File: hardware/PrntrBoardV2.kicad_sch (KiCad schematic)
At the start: 13 parts

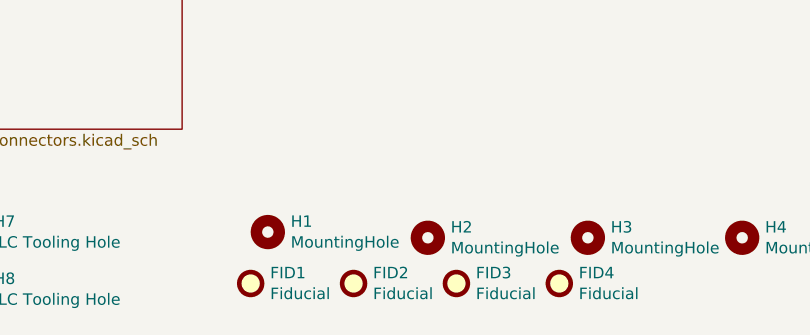
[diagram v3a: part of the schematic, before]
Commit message: Added separate power supply for motor drivers, to accomodate high voltage driver versions.
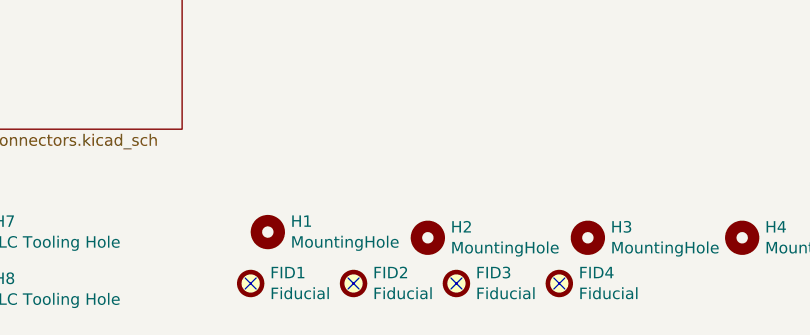
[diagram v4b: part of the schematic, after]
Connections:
- no-connect marks 0 -> 4
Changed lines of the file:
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@@
 (kicad_sch (version 20210621) (generator eeschema)
   (paper "A4")
+  (no_connect (at 196.215 157.48))
+  (no_connect (at 207.645 157.48))
+  (no_connect (at 219.075 157.48))
+  (no_connect (at 230.505 157.48))
   (symbol (lib_id "Mechanical:Fiducial") (at 196.215 157.48 0) (unit 1)
     (in_bom no) (on_board yes)
@@
       (reference "#PWR077") (unit 1) (value "GND") (footprint "")
     )
+    (path "/00000000-0000-0000-0000-00005db03b7d/9aa42597-a571-49ba-a769-f65a412defcf"
+      (reference "#PWR078") (unit 1) (value "GND") (footprint "")
+    )
+    (path "/00000000-0000-0000-0000-00005db03b7d/f7e58a64-e7a2-485d-858e-ff6a326b8d61"
+      (reference "#PWR079") (unit 1) (value "GND") (footprint "")
+    )
     (path "/00000000-0000-0000-0000-00005dabbbab/00000000-0000-0000-0000-00005daf7240"
       (reference "#PWR0101") (unit 1) (value "GND") (footprint "")
@@
       (reference "#PWR0104") (unit 1) (value "GND") (footprint "")
     )
+    (path "/00000000-0000-0000-0000-00005dabbbab/8844a2b1-600f-4d16-a024-4570839840b9"
+      (reference "#PWR0105") (unit 1) (value "GNDA") (footprint "")
+    )
     (path "/00000000-0000-0000-0000-00005dabbbab/00000000-0000-0000-0000-00005dabc8ef"
       (reference "C1") (unit 1) (value "0.1uF") (footprint "PrntrBoardV2:C_0603_1608Metric")
@@
       (reference "C46") (unit 1) (value "0.1uF") (footprint "PrntrBoardV2:C_0603_1608Metric")
     )
-    (path "/00000000-0000-0000-0000-00005dace5fc/00000000-0000-0000-0000-00005db2f31b"
-      (reference "C47") (unit 1) (value "100uF 35V") (footprint "Capacitor_SMD:CP_Elec_6.3x7.7")
-    )
-    (path "/00000000-0000-0000-0000-00005dace5fc/00000000-0000-0000-0000-00005db33ffa"
-      (reference "C48") (unit 1) (value "100uF 35V") (footprint "Capacitor_SMD:CP_Elec_6.3x7.7")
-    )
-    (path "/00000000-0000-0000-0000-00005dace5fc/00000000-0000-0000-0000-00005db326a1"
-      (reference "C49") (unit 1) (value "100uF 35V") (footprint "Capacitor_SMD:CP_Elec_6.3x7.7")
-    )
-    (path "/00000000-0000-0000-0000-00005dace5fc/00000000-0000-0000-0000-00005db3478c"
-      (reference "C50") (unit 1) (value "100uF 35V") (footprint "Capacitor_SMD:CP_Elec_6.3x7.7")
-    )
-    (path "/00000000-0000-0000-0000-00005dace5fc/00000000-0000-0000-0000-00005db32f14"
-      (reference "C51") (unit 1) (value "100uF 35V") (footprint "Capacitor_SMD:CP_Elec_6.3x7.7")
-    )
-    (path "/00000000-0000-0000-0000-00005dace5fc/00000000-0000-0000-0000-00005db339e2"
-      (reference "C52") (unit 1) (value "100uF 35V") (footprint "Capacitor_SMD:CP_Elec_6.3x7.7")
+    (path "/00000000-0000-0000-0000-00005dace5fc/f1cb98d4-956f-4cdb-a90e-6df52427c521"
+      (reference "C47") (unit 1) (value "4.7uF 100V") (footprint "Capacitor_SMD:C_1210_3225Metric")
+    )
+    (path "/00000000-0000-0000-0000-00005dace5fc/c30c9426-6699-4791-b9e2-3fdd8b988993"
+      (reference "C48") (unit 1) (value "4.7uF 100V") (footprint "Capacitor_SMD:C_1210_3225Metric")
+    )
+    (path "/00000000-0000-0000-0000-00005dace5fc/caba8d8c-9e30-4f2a-ac28-2592b6bac444"
+      (reference "C49") (unit 1) (value "4.7uF 100V") (footprint "Capacitor_SMD:C_1210_3225Metric")
+    )
+    (path "/00000000-0000-0000-0000-00005dace5fc/72709611-bead-4d14-a8e4-96cb6435ce79"
+      (reference "C50") (unit 1) (value "4.7uF 100V") (footprint "Capacitor_SMD:C_1210_3225Metric")
+    )
+    (path "/00000000-0000-0000-0000-00005dace5fc/a6c99147-871a-4a25-9990-e43f4c1d423e"
+      (reference "C51") (unit 1) (value "4.7uF 100V") (footprint "Capacitor_SMD:C_1210_3225Metric")
+    )
+    (path "/00000000-0000-0000-0000-00005dace5fc/ba0f645d-236d-4590-bcc3-0a7e6362da74"
+      (reference "C52") (unit 1) (value "4.7uF 100V") (footprint "Capacitor_SMD:C_1210_3225Metric")
     )
     (path "/00000000-0000-0000-0000-00005dabbbab/00000000-0000-0000-0000-00005eb800bd"
@@
       (reference "D33") (unit 1) (value "B5819W") (footprint "Diode_SMD:D_SOD-123")
     )
+    (path "/00000000-0000-0000-0000-00005db03b7d/71e29ebc-bf9c-4e9a-b3ba-643697a383eb"
+      (reference "D34") (unit 1) (value "LED") (footprint "PrntrBoardV2:LED_0603_1608Metric")
+    )
+    (path "/00000000-0000-0000-0000-00005db03b7d/ee51799c-0a52-4e42-8e1b-9fbd2a8e51a7"
+      (reference "D35") (unit 1) (value "10V") (footprint "Diode_SMD:D_SOD-323")
+    )
     (path "/00000000-0000-0000-0000-00005daf0ef9/00000000-0000-0000-0000-00005db1f945"
       (reference "EXP1") (unit 1) (value "IDC 2x5") (footprint "Connector_IDC:IDC-Header_2x05_P2.54mm_Vertical")
@@
       (reference "F3") (unit 1) (value "Fuse") (footprint "PrntrBoardV2:2410_FuseFolder")
     )
-    (path "/00000000-0000-0000-0000-00005db03b7d/00000000-0000-0000-0000-00005db106e6"
+    (path "/00000000-0000-0000-0000-00005db03b7d/2bd93e06-617d-4738-9f15-bf8608503da7"
       (reference "F4") (unit 1) (value "Fuse") (footprint "PrntrBoardV2:2410_FuseFolder")
     )
@@
       (reference "J1") (unit 1) (value "JST XH") (footprint "Connector_JST:JST_XH_B2B-XH-A_1x02_P2.50mm_Vertical")
     )
-    (path "/00000000-0000-0000-0000-00005db03b7d/00000000-0000-0000-0000-00005dbab4bc"
-      (reference "J2") (unit 1) (value "JST XH") (footprint "Connector_JST:JST_XH_B2B-XH-A_1x02_P2.50mm_Vertical")
-    )
     (path "/00000000-0000-0000-0000-00005daf0ef9/00000000-0000-0000-0000-00005daf169f"
       (reference "J3") (unit 1) (value "USB_B_Micro") (footprint "PrntrBoardV2:MC-101C")
@@
       (reference "J25") (unit 1) (value "JST XH") (footprint "Connector_JST:JST_XH_B2B-XH-A_1x02_P2.50mm_Vertical")
     )
-    (path "/00000000-0000-0000-0000-00005db03b7d/00000000-0000-0000-0000-00005dc26f16"
-      (reference "J26") (unit 1) (value "JST XH") (footprint "Connector_JST:JST_XH_B2B-XH-A_1x02_P2.50mm_Vertical")
-    )
     (path "/00000000-0000-0000-0000-00005db03b7d/00000000-0000-0000-0000-00005dc277af"
       (reference "J27") (unit 1) (value "JST XH") (footprint "Connector_JST:JST_XH_B2B-XH-A_1x02_P2.50mm_Vertical")
     )
-    (path "/00000000-0000-0000-0000-00005db03b7d/b3a465ad-aba6-44c4-a415-44cf38e5153b"
-      (reference "J28") (unit 1) (value "KF350") (footprint "PrntrBoardV2:TerminalBlock_Phoenix_PT-1,5-2-3.5-H_1x02_P3.50mm_Horizontal")
+    (path "/00000000-0000-0000-0000-00005db03b7d/2d4cb065-feb1-41b6-9a37-fb4f85c805ba"
+      (reference "J28") (unit 1) (value "KF129") (footprint "PrntrBoardV2:TerminalBlock_Phoenix_MKDS-1,5-2-5.08_1x02_P5.08mm_Horizontal")
     )
     (path "/00000000-0000-0000-0000-00005daf0ef9/967818d5-7083-4d03-b3d3-4a38bcfd269b"
       (reference "J29") (unit 1) (value "RJ12_Shielded") (footprint "Connector_RJ:RJ12_Amphenol_54601")
     )
+    (path "/00000000-0000-0000-0000-00005db03b7d/dbcab08d-345c-4d98-bc4f-c670560350fc"
+      (reference "J30") (unit 1) (value "KF129") (footprint "PrntrBoardV2:TerminalBlock_Phoenix_MKDS-1,5-2-5.08_1x02_P5.08mm_Horizontal")
+    )
     (path "/00000000-0000-0000-0000-00005daf0ef9/00000000-0000-0000-0000-00005db37293"
       (reference "JP1") (unit 1) (value "Jumper_2_Open") (footprint "Connector_PinHeader_2.54mm:PinHeader_1x02_P2.54mm_Vertical")
@@
       (reference "J_Z-1") (unit 1) (value "JST XH 3p") (footprint "Connector_JST:JST_XH_B3B-XH-A_1x03_P2.50mm_Vertical")
     )
-    (path "/00000000-0000-0000-0000-00005db03b7d/00000000-0000-0000-0000-00005db0c404"
-      (reference "J_power_in1") (unit 1) (value "KF635") (footprint "TerminalBlock_MetzConnect:TerminalBlock_MetzConnect_Type701_RT11L02HGLU_1x02_P6.35mm_Horizontal")
-    )
     (path "/00000000-0000-0000-0000-00005dab51d1"
       (reference "LOGO1") (unit 1) (value "Logo_Open_Hardware_Small") (footprint "Symbol:OSHW-Logo2_9.8x8mm_SilkScreen")
@@
       (reference "Q1") (unit 1) (value "NCE40P40K") (footprint "Package_TO_SOT_SMD:TO-252-2")
     )
+    (path "/00000000-0000-0000-0000-00005db03b7d/93cefafd-207a-42a8-96ac-191179289d1b"
+      (reference "Q2") (unit 1) (value "SQM110P06-8M9L") (footprint "Package_TO_SOT_SMD:TO-252-2")
+    )
     (path "/00000000-0000-0000-0000-00005dabbbab/00000000-0000-0000-0000-00005dabc8f8"
       (reference "R1") (unit 1) (value "10k") (footprint "PrntrBoardV2:R_0603_1608Metric")
@@
       (reference "R3") (unit 1) (value "10k") (footprint "PrntrBoardV2:R_0603_1608Metric")
     )
+    (path "/00000000-0000-0000-0000-00005db03b7d/fc56f2f4-f120-4c15-a4d5-860fedfd0873"
+      (reference "R4") (unit 1) (value "27k") (footprint "PrntrBoardV2:R_0603_1608Metric")
+    )
     (path "/00000000-0000-0000-0000-00005dabbbab/00000000-0000-0000-0000-00005dabc8f6"
       (reference "R5") (unit 1) (value "10k") (footprint "PrntrBoardV2:R_0603_1608Metric")
@@
       (reference "R78") (unit 1) (value "10k") (footprint "PrntrBoardV2:R_0603_1608Metric")
     )
+    (path "/00000000-0000-0000-0000-00005db03b7d/efb47e74-9f4a-4123-bbc0-a515f517b3ce"
+      (reference "R79") (unit 1) (value "100k") (footprint "PrntrBoardV2:R_0603_1608Metric")
+    )
     (path "/00000000-0000-0000-0000-00005daf0ef9/00000000-0000-0000-0000-00005db1f947"
